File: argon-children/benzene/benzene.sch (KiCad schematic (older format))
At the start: 9 parts, among them U1 Conn1, U2 SPI FLASH, U3 Conn2

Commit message: Add 555 to benzene
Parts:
- added C3: 10uF, symbol Device:C
- added C4: 1uF, symbol Device:CP1
- added D1: LED, symbol Device:LED
- added R5: 1.5K, symbol Device:R
- added R6: 330R, symbol Device:R
- added R7: 100K, symbol Device:R
- added U4: LMC555, Package_SO:SOIC-8_3.9x4.9mm_P1.27mm, symbol Timer:LMC555xM
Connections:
- net at C1.1, C2.1, U1.1 (V3V3)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: now also R5.2, U4.8 (VCC)
- net at C1.2, C2.2, U1.2 (GND)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: now also C3.2, C4.2, D1.1 (K), U4.1 (GND)
- net ~CS: now reaches R1.2, U3.4 (MISO)
- net ~CS: now also R5.1, U4.2 (TR)
- new net: R6.1, U4.3 (Q)
- new net: C3.1, U4.5 (CV)
- new net: C4.1, R7.2, U4.6 (THR), U4.7 (DIS)
- new net: D1.2 (A), R6.2
- new net V3V3: R7.1, U4.4 (R)
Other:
- moved on the sheet: C1, C2, R1, R2, R3, R4, U1, U2, U3

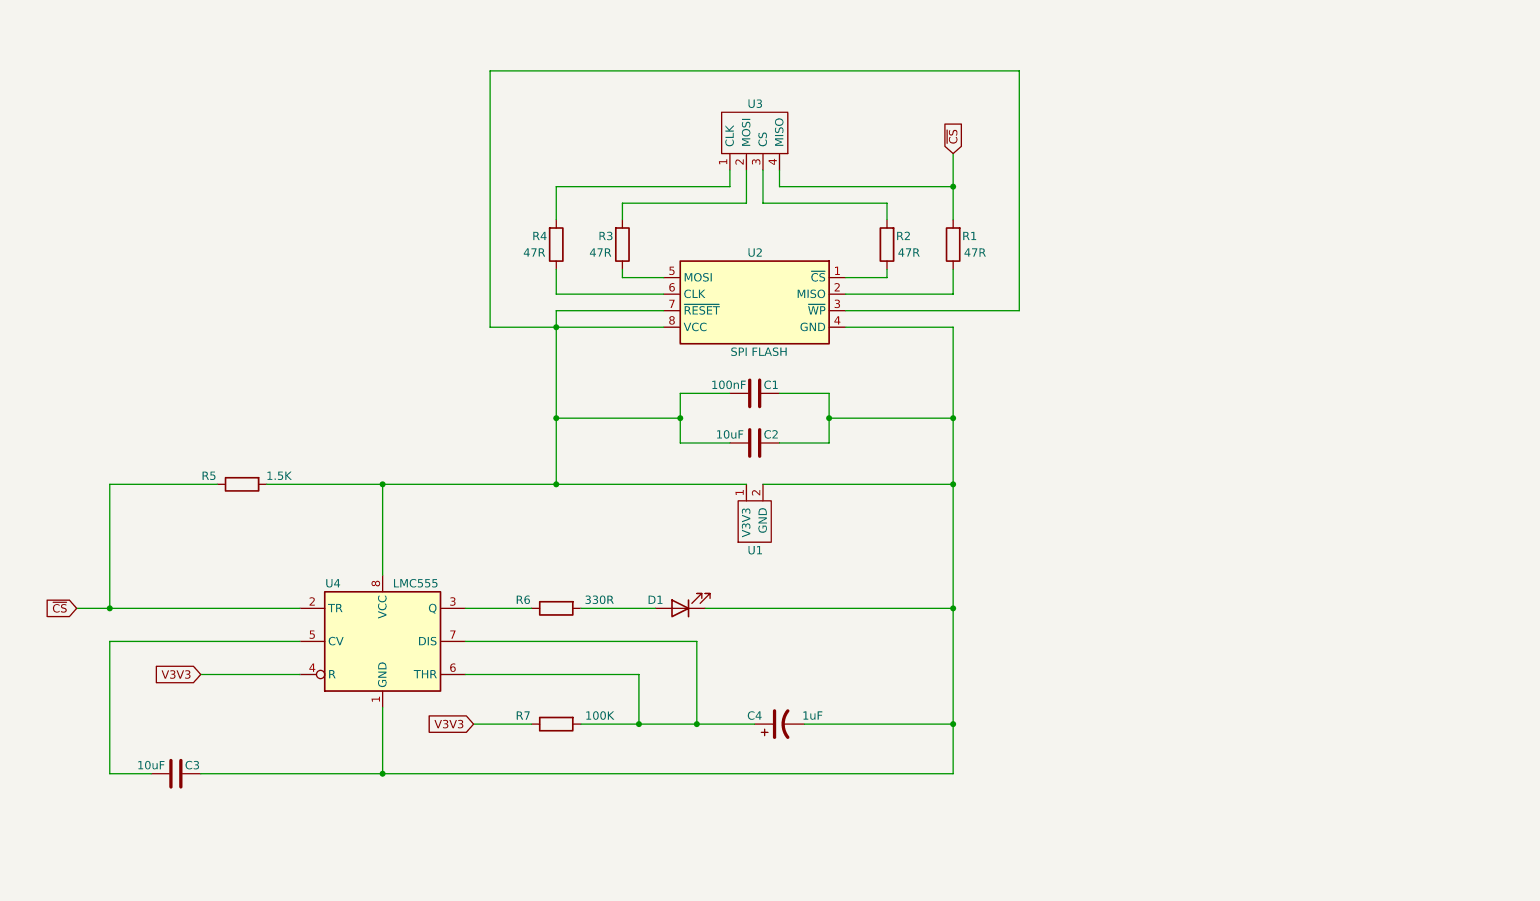
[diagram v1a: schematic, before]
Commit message: Benzene & 555 - redraw to two schemas
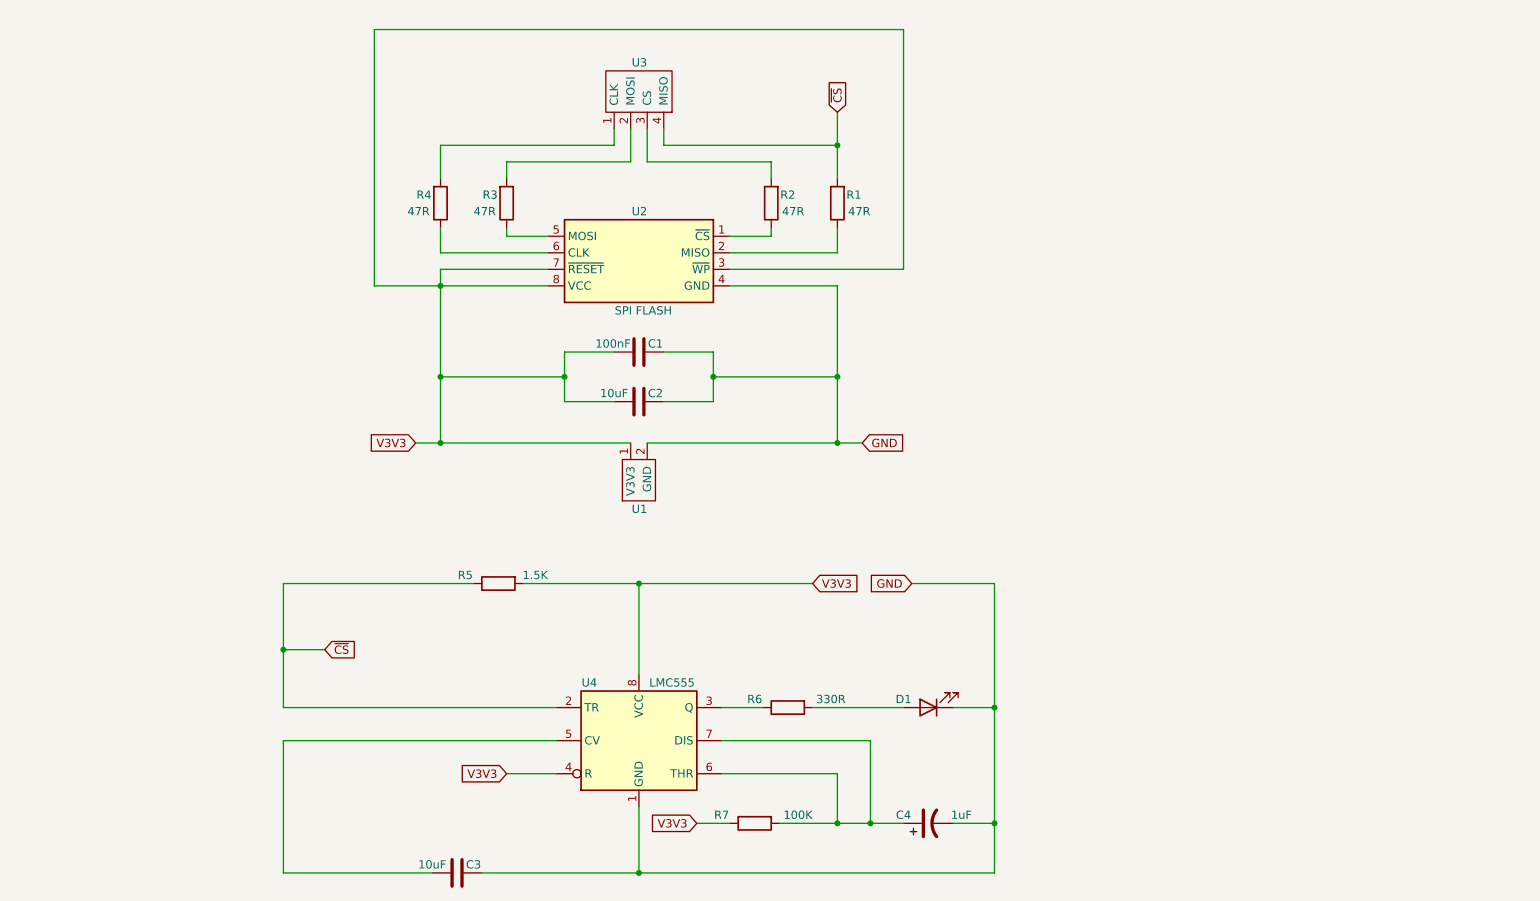
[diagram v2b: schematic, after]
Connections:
- net V3V3: now also C1.1, C2.1, R5.2, U1.1 (V3V3), U2.3 (~WP), U2.7 (~RESET), U2.8 (VCC), U4.8 (VCC)
- net GND: now reaches C1.2, C2.2, C3.2, C4.2, D1.1 (K), U1.2 (GND), U2.4 (GND), U4.1 (GND)
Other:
- moved on the sheet: C1, C2, C3, C4, D1, R1, R2, R3, R4, R5, R6, R7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

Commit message: Benzene footprints
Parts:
- C1, C2, C3, C4: footprint (none) -> Capacitor_SMD:C_0603_1608Metric
- D1: footprint (none) -> LED_SMD:LED_0805_2012Metric
- R1, R2, R3, R4, R5, R6, R7: footprint (none) -> Resistor_SMD:R_0603_1608Metric
- U1: footprint (none) -> Connector_PinHeader_2.54mm:PinHeader_1x02_P2.54mm_Vertical
- U2: footprint Package_SO:SOP-8_3.9x4.9mm_P1.27mm -> Package_DIP:DIP-8_W7.62mm_Socket
- U3: footprint (none) -> Connector_PinHeader_2.54mm:PinHeader_1x04_P2.54mm_Vertical
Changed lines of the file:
@@
 F 0 "U2" H 5800 2850 50  0000 L CNN
 F 1 "SPI FLASH" H 5650 2250 50  0000 L CNN
-F 2 "Package_SO:SOP-8_3.9x4.9mm_P1.27mm" H 5850 1900 50  0001 C CNN
+F 2 "Package_DIP:DIP-8_W7.62mm_Socket" H 5850 1900 50  0001 C CNN
 F 3 "http://www.macronix.com/Lists/Datasheet/Attachments/7534/MX25R3235F,%20Wide%20Range,%2032Mb,%20v1.6.pdf" H 5850 2500 50  0001 C CNN
 	1    5850 2500
@@
 F 0 "U1" V 6100 3750 50  0000 L CNN
 F 1 "Conn1" V 5912 3938 50  0001 L CNN
-F 2 "" H 5800 4050 50  0001 C CNN
+F 2 "Connector_PinHeader_2.54mm:PinHeader_1x02_P2.54mm_Vertical" H 5800 4050 50  0001 C CNN
 F 3 "" H 5800 4050 50  0001 C CNN
 	1    5900 3750
@@
 F 0 "R3" H 4950 2050 50  0000 C CNN
 F 1 "47R" H 4850 2150 50  0000 L CNN
-F 2 "" V 4980 2100 50  0001 C CNN
+F 2 "Resistor_SMD:R_0603_1608Metric" V 4980 2100 50  0001 C CNN
 F 3 "~" H 5050 2100 50  0001 C CNN
 	1    5050 2100
@@
 F 0 "R4" H 4550 2050 50  0000 C CNN
 F 1 "47R" H 4450 2150 50  0000 L CNN
-F 2 "" V 4580 2100 50  0001 C CNN
+F 2 "Resistor_SMD:R_0603_1608Metric" V 4580 2100 50  0001 C CNN
 F 3 "~" H 4650 2100 50  0001 C CNN
 	1    4650 2100
@@
 F 0 "R2" H 6550 2050 50  0000 C CNN
 F 1 "47R" H 6450 2150 50  0000 L CNN
-F 2 "" V 6580 2100 50  0001 C CNN
+F 2 "Resistor_SMD:R_0603_1608Metric" V 6580 2100 50  0001 C CNN
 F 3 "~" H 6650 2100 50  0001 C CNN
 	1    6650 2100
@@
 F 0 "R1" H 6950 2050 50  0000 C CNN
 F 1 "47R" H 6850 2150 50  0000 L CNN
-F 2 "" V 6980 2100 50  0001 C CNN
+F 2 "Resistor_SMD:R_0603_1608Metric" V 6980 2100 50  0001 C CNN
 F 3 "~" H 7050 2100 50  0001 C CNN
 	1    7050 2100
@@
 F 0 "U3" V 5700 1450 50  0000 R CNN
 F 1 "Conn2" V 5750 950 50  0001 R CNN
-F 2 "" H 5700 1650 50  0001 C CNN
+F 2 "Connector_PinHeader_2.54mm:PinHeader_1x04_P2.54mm_Vertical" H 5700 1650 50  0001 C CNN
 F 3 "" H 5700 1650 50  0001 C CNN
 	1    5800 1350
@@
 F 0 "C1" V 5800 2900 50  0000 C CNN
 F 1 "100nF" V 5800 3050 50  0000 L CNN
-F 2 "" H 5888 2850 50  0001 C CNN
+F 2 "Capacitor_SMD:C_0603_1608Metric" H 5888 2850 50  0001 C CNN
 F 3 "~" H 5850 3000 50  0001 C CNN
 	1    5850 3000
@@
 F 0 "C2" V 5800 3200 50  0000 C CNN
 F 1 "10uF" V 5800 3450 50  0000 C CNN
-F 2 "" H 5888 3150 50  0001 C CNN
+F 2 "Capacitor_SMD:C_0603_1608Metric" H 5888 3150 50  0001 C CNN
 F 3 "~" H 5850 3300 50  0001 C CNN
 	1    5850 3300
@@
 F 0 "R7" V 6500 6050 50  0000 C CNN
 F 1 "100K" V 6500 5500 50  0000 L CNN
-F 2 "" V 6480 5850 50  0001 C CNN
+F 2 "Resistor_SMD:R_0603_1608Metric" V 6480 5850 50  0001 C CNN
 F 3 "~" H 6550 5850 50  0001 C CNN
 	1    6550 5850
@@
 F 0 "D1" H 7750 5100 50  0000 C CNN
 F 1 "LED" H 7650 5300 50  0001 C CNN
-F 2 "" H 7600 5150 50  0001 C CNN
+F 2 "LED_SMD:LED_0805_2012Metric" H 7600 5150 50  0001 C CNN
 F 3 "~" H 7600 5150 50  0001 C CNN
 	1    7600 5150
@@
 F 0 "C4" V 7650 6000 50  0000 C CNN
 F 1 "1uF" V 7650 5650 50  0000 C CNN
-F 2 "" H 7600 5850 50  0001 C CNN
+F 2 "Capacitor_SMD:C_0603_1608Metric" H 7600 5850 50  0001 C CNN
 F 3 "~" H 7600 5850 50  0001 C CNN
 	1    7600 5850
@@
 F 0 "R6" V 6700 5350 50  0000 C CNN
 F 1 "330R" V 6700 4800 50  0000 L CNN
-F 2 "" V 6680 5150 50  0001 C CNN
+F 2 "Resistor_SMD:R_0603_1608Metric" V 6680 5150 50  0001 C CNN
 F 3 "~" H 6750 5150 50  0001 C CNN
 	1    6750 5150
@@
 F 0 "R5" V 4950 4600 50  0000 C CNN
 F 1 "1.5K" V 4950 4100 50  0000 L CNN
-F 2 "" V 4930 4400 50  0001 C CNN
+F 2 "Resistor_SMD:R_0603_1608Metric" V 4930 4400 50  0001 C CNN
 F 3 "~" H 5000 4400 50  0001 C CNN
 	1    5000 4400
@@
 F 0 "C3" V 4700 6050 50  0000 C CNN
 F 1 "10uF" V 4700 6300 50  0000 C CNN
-F 2 "" H 4788 6000 50  0001 C CNN
+F 2 "Capacitor_SMD:C_0603_1608Metric" H 4788 6000 50  0001 C CNN
 F 3 "~" H 4750 6150 50  0001 C CNN
 	1    4750 6150

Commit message: Benzene - PCB, part 1
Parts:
- added H1, H2, H3, H4: MountingHole, MountingHole:MountingHole_3.2mm_M3, symbol Mechanical:MountingHole
- U4: footprint Package_SO:SOIC-8_3.9x4.9mm_P1.27mm -> Package_SO:VSSOP-8_3.0x3.0mm_P0.65mm
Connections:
- net ~CS: now also R2.2, U3.3 (CS); no longer R1.2, U3.4 (MISO)
- new net: R1.2, U3.4 (MISO)
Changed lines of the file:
@@
 Wire Wire Line
 	7450 5850 7250 5850
-Wire Wire Line
-	7050 1750 7050 1550
-Connection ~ 7050 1750
-Text GLabel 7050 1550 1    50   Input ~ 0
+Text GLabel 6750 1850 2    50   Input ~ 0
 ~CS
 $Comp
@@
 F 0 "U4" H 5550 5700 50  0000 C CNN
 F 1 "LMC555" H 6050 5700 50  0000 C CNN
-F 2 "Package_SO:SOIC-8_3.9x4.9mm_P1.27mm" H 6700 4950 50  0001 C CNN
+F 2 "Package_SO:VSSOP-8_3.0x3.0mm_P0.65mm" H 6700 4950 50  0001 C CNN
 F 3 "http://www.ti.com/lit/ds/symlink/lmc555.pdf" H 6700 4950 50  0001 C CNN
 	1    5850 5350
@@
 	7200 3550 7050 3550
 Connection ~ 7050 3550
+Wire Wire Line
+	6750 1850 6650 1850
+Connection ~ 6650 1850
+$Comp
+L Mechanical:MountingHole H1
+U 1 1 5FD67913
+P 10500 5150
+F 0 "H1" H 10600 5196 50  0000 L CNN
+F 1 "MountingHole" H 10600 5105 50  0000 L CNN
+F 2 "MountingHole:MountingHole_3.2mm_M3" H 10500 5150 50  0001 C CNN
+F 3 "~" H 10500 5150 50  0001 C CNN
+	1    10500 5150
+	1    0    0    -1
+$EndComp
+$Comp
+L Mechanical:MountingHole H2
+U 1 1 5FD67E8D
+P 10500 5400
+F 0 "H2" H 10600 5446 50  0000 L CNN
+F 1 "MountingHole" H 10600 5355 50  0000 L CNN
+F 2 "MountingHole:MountingHole_3.2mm_M3" H 10500 5400 50  0001 C CNN
+F 3 "~" H 10500 5400 50  0001 C CNN
+	1    10500 5400
+	1    0    0    -1
+$EndComp
+$Comp
+L Mechanical:MountingHole H3
+U 1 1 5FD680BA
+P 10500 5650
+F 0 "H3" H 10600 5696 50  0000 L CNN
+F 1 "MountingHole" H 10600 5605 50  0000 L CNN
+F 2 "MountingHole:MountingHole_3.2mm_M3" H 10500 5650 50  0001 C CNN
+F 3 "~" H 10500 5650 50  0001 C CNN
+	1    10500 5650
+	1    0    0    -1
+$EndComp
+$Comp
+L Mechanical:MountingHole H4
+U 1 1 5FD681EC
+P 10500 5900
+F 0 "H4" H 10600 5946 50  0000 L CNN
+F 1 "MountingHole" H 10600 5855 50  0000 L CNN
+F 2 "MountingHole:MountingHole_3.2mm_M3" H 10500 5900 50  0001 C CNN
+F 3 "~" H 10500 5900 50  0001 C CNN
+	1    10500 5900
+	1    0    0    -1
+$EndComp
 $EndSCHEMATC

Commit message: Benzene
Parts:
- removed H1, H2, H3, H4: MountingHole, MountingHole:MountingHole_3.2mm_M3, symbol Mechanical:MountingHole
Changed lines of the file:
@@
 	6750 1850 6650 1850
 Connection ~ 6650 1850
-$Comp
-L Mechanical:MountingHole H1
-U 1 1 5FD67913
-P 10500 5150
-F 0 "H1" H 10600 5196 50  0000 L CNN
-F 1 "MountingHole" H 10600 5105 50  0000 L CNN
-F 2 "MountingHole:MountingHole_3.2mm_M3" H 10500 5150 50  0001 C CNN
-F 3 "~" H 10500 5150 50  0001 C CNN
-	1    10500 5150
-	1    0    0    -1
-$EndComp
-$Comp
-L Mechanical:MountingHole H2
-U 1 1 5FD67E8D
-P 10500 5400
-F 0 "H2" H 10600 5446 50  0000 L CNN
-F 1 "MountingHole" H 10600 5355 50  0000 L CNN
-F 2 "MountingHole:MountingHole_3.2mm_M3" H 10500 5400 50  0001 C CNN
-F 3 "~" H 10500 5400 50  0001 C CNN
-	1    10500 5400
-	1    0    0    -1
-$EndComp
-$Comp
-L Mechanical:MountingHole H3
-U 1 1 5FD680BA
-P 10500 5650
-F 0 "H3" H 10600 5696 50  0000 L CNN
-F 1 "MountingHole" H 10600 5605 50  0000 L CNN
-F 2 "MountingHole:MountingHole_3.2mm_M3" H 10500 5650 50  0001 C CNN
-F 3 "~" H 10500 5650 50  0001 C CNN
-	1    10500 5650
-	1    0    0    -1
-$EndComp
-$Comp
-L Mechanical:MountingHole H4
-U 1 1 5FD681EC
-P 10500 5900
-F 0 "H4" H 10600 5946 50  0000 L CNN
-F 1 "MountingHole" H 10600 5855 50  0000 L CNN
-F 2 "MountingHole:MountingHole_3.2mm_M3" H 10500 5900 50  0001 C CNN
-F 3 "~" H 10500 5900 50  0001 C CNN
-	1    10500 5900
-	1    0    0    -1
-$EndComp
 $EndSCHEMATC

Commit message: Benzene refactored
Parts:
- U2: footprint Package_DIP:DIP-8_W7.62mm_Socket -> benzene:DIP-8_W7.62mm_Socket
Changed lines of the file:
@@
 F 0 "U2" H 5800 2850 50  0000 L CNN
 F 1 "SPI FLASH" H 5650 2250 50  0000 L CNN
-F 2 "Package_DIP:DIP-8_W7.62mm_Socket" H 5850 1900 50  0001 C CNN
+F 2 "benzene:DIP-8_W7.62mm_Socket" H 5850 1900 50  0001 C CNN
 F 3 "http://www.macronix.com/Lists/Datasheet/Attachments/7534/MX25R3235F,%20Wide%20Range,%2032Mb,%20v1.6.pdf" H 5850 2500 50  0001 C CNN
 	1    5850 2500
